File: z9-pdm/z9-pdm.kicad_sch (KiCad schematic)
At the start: 8 parts

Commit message: Refactor junctions and wires in connectors schematic; remove unused labels and pins in z9-pdm schematic; update project settings to ignore four-way junction warnings; enhance ERC settings in shared project configuration.
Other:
- sheet power ports: added none; removed +5V_ISO, GND_ISO
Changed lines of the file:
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@@
-		)
-	)
-	(label "+5V_ISO"
-		(at 92.71 143.51 0)
-		(effects
-			(font
-				(size 1.27 1.27)
-			)
-			(justify left bottom)
 		)
 	)
@@
 			)
 			(justify right bottom)
-		)
-	)
-	(label "GND_ISO"
-		(at 92.71 149.86 0)
-		(effects
-			(font
-				(size 1.27 1.27)
-			)
-			(justify left bottom)
 		)
 	)
@@
 			)
 		)
-		(pin "GND_ISO" input
-			(at 92.71 149.86 0)
-			(effects
-				(font
-					(size 1.27 1.27)
-				)
-				(justify right)
-			)
-		)
-		(pin "+5V_ISO" output
-			(at 92.71 143.51 0)
-			(effects
-				(font
-					(size 1.27 1.27)
-				)
-				(justify right)
-			)
-		)

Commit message: pre replicate analogue chans
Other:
- sheet shared_usb renamed shared_usbc
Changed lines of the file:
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@@
 			(project "z9-pdm"
 				(path "/b643db5c-578e-4b48-aafc-cc4190db582a"
-					(page "11")
+					(page "49")
 				)
 			)
@@
 			(color 0 0 0 0.0000)
 		)
-		(property "Sheetname" "shared_usb"
+		(property "Sheetname" "shared_usbc"
 			(at 52.07 196.1384 0)
 			(effects

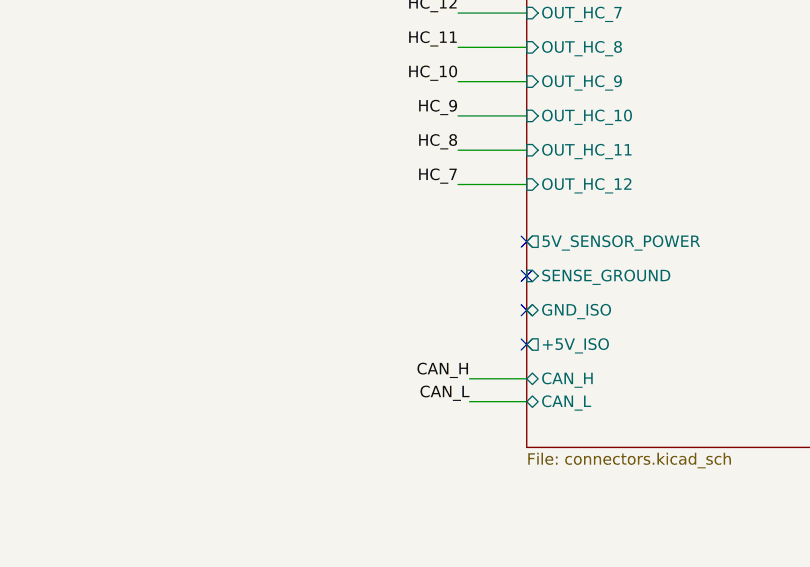
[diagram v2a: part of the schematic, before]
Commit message: laypout ad section canl/h swap
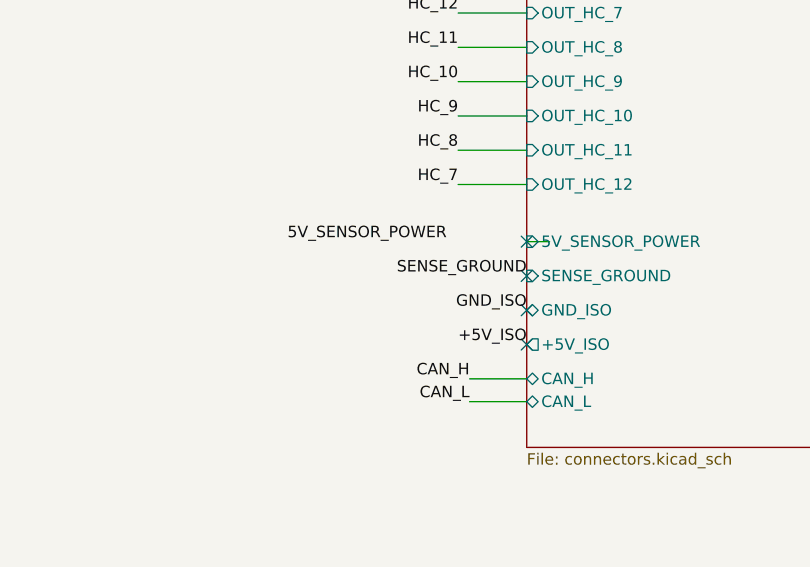
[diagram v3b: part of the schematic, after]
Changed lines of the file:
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@@
+	)
+	(no_connect
+		(at 191.77 158.75)
+	)
+	(no_connect
+		(at 191.77 91.44)
+	)
+	(no_connect
+		(at 191.77 99.06)
+	)
+	(no_connect
+		(at 312.42 91.44)
+	)
+	(no_connect
+		(at 191.77 96.52)
+	)
+	(no_connect
+		(at 312.42 87.63)
+	)
+	(no_connect
+		(at 191.77 88.9)
+	)
+	(no_connect
+		(at 191.77 101.6)
+	)
+	(no_connect
+		(at 191.77 170.18)
+	)
+	(no_connect
+		(at 191.77 151.13)
+	)
+	(no_connect
+		(at 160.02 78.74)
+	)
+	(no_connect
+		(at 191.77 165.1)
+	)
+	(no_connect
+		(at 191.77 156.21)
+	)
+	(no_connect
+		(at 191.77 148.59)
+	)
+	(no_connect
+		(at 191.77 161.29)
+	)
+	(no_connect
+		(at 191.77 153.67)
 	)
 	(no_connect
 		(at 312.42 83.82)
-	)
-	(no_connect
-		(at 191.77 158.75)
-	)
-	(no_connect
-		(at 191.77 91.44)
-	)
-	(no_connect
-		(at 191.77 99.06)
-	)
-	(no_connect
-		(at 312.42 91.44)
-	)
-	(no_connect
-		(at 191.77 96.52)
-	)
-	(no_connect
-		(at 312.42 87.63)
-	)
-	(no_connect
-		(at 191.77 88.9)
-	)
-	(no_connect
-		(at 191.77 101.6)
-	)
-	(no_connect
-		(at 191.77 170.18)
-	)
-	(no_connect
-		(at 191.77 151.13)
-	)
-	(no_connect
-		(at 160.02 78.74)
-	)
-	(no_connect
-		(at 191.77 165.1)
-	)
-	(no_connect
-		(at 191.77 156.21)
-	)
-	(no_connect
-		(at 191.77 148.59)
-	)
-	(no_connect
-		(at 191.77 161.29)
-	)
-	(no_connect
-		(at 191.77 153.67)
 	)
 	(no_connect
@@
 	(wire
 		(pts
-			(xy 304.8 54.61) (xy 312.42 54.61)
+			(xy 312.42 83.82) (xy 314.96 83.82)
 		)
 		(stroke
@@
 		)
 	)
+	(wire
+		(pts
+			(xy 304.8 54.61) (xy 312.42 54.61)
+		)
+		(stroke
+			(width 0)
+			(type default)
+		)
+	)
 	(label "CAN_L"
 		(at 306.07 101.6 180)
@@
 		)
 	)
+	(label "SENSE_GROUND"
+		(at 312.42 87.63 180)
+		(effects
+			(font
+				(size 1.27 1.27)
+			)
+			(justify right bottom)
+		)
+	)
 	(label "USB_OTG_FS_DP"
 		(at 160.02 31.75 180)
@@
 		)
 	)
+	(label "5V_SENSOR_POWER"
+		(at 303.53 83.82 180)
+		(effects
+			(font
+				(size 1.27 1.27)
+			)
+			(justify right bottom)
+		)
+	)
 	(label "HC_5"
 		(at 304.8 39.37 180)
@@
 		)
 	)
+	(label "GND_ISO"
+		(at 312.42 91.44 180)
+		(effects
+			(font
+				(size 1.27 1.27)
+			)
+			(justify right bottom)
+		)
+	)
 	(label "SENSE_8"
 		(at 363.22 53.34 0)
@@
 	(label "TIM1_CH3"
 		(at 52.07 179.07 180)
+		(effects
+			(font
+				(size 1.27 1.27)
+			)
+			(justify right bottom)
+		)
+	)
+	(label "+5V_ISO"
+		(at 312.42 95.25 180)
 		(effects
 			(font
@@
 			)
 		)
-		(pin "5V_SENSOR_POWER" output
+		(pin "5V_SENSOR_POWER" input
 			(at 312.42 83.82 180)
 			(effects
